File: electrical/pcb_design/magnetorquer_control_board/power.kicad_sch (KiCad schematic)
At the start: 10 parts, among them J4 External Power, U5 INA260, U6 TLV76733DRVx

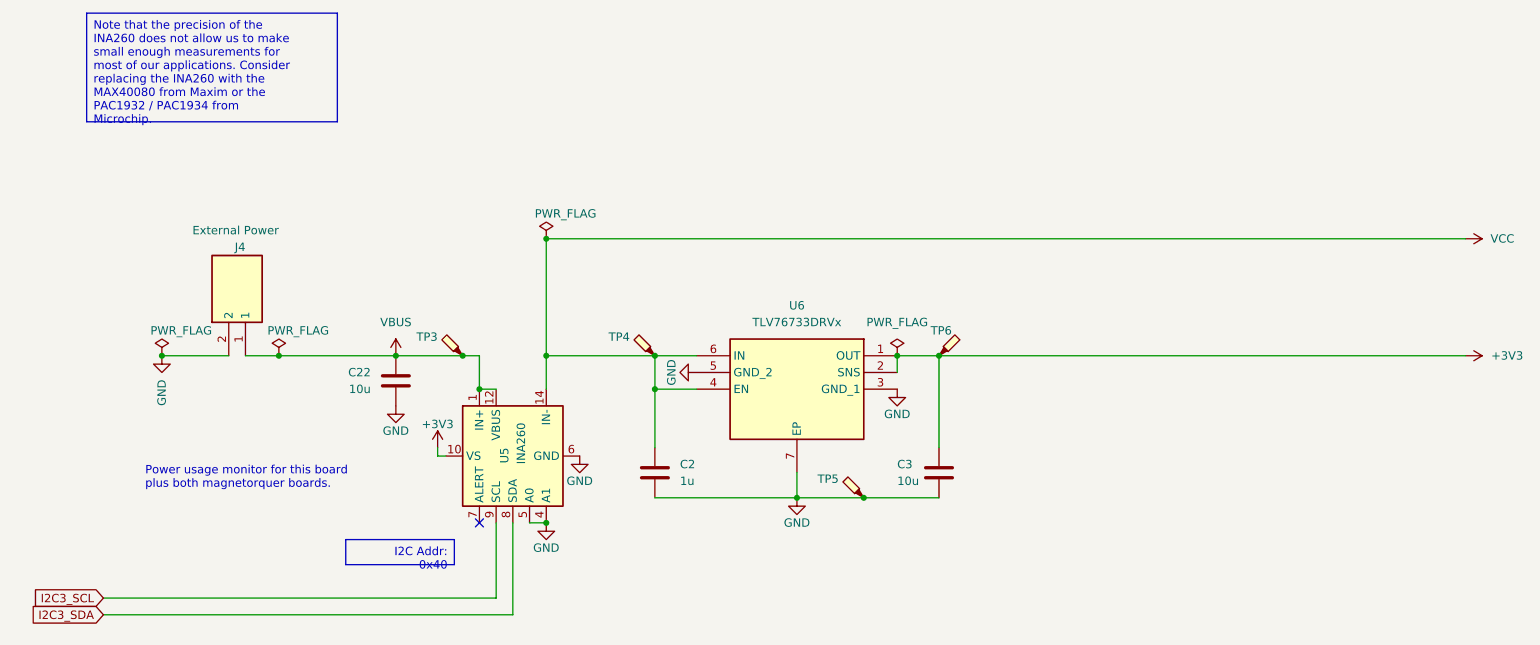
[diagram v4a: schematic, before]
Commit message: Restructure schematic pages. Update designs based on discussions with team.
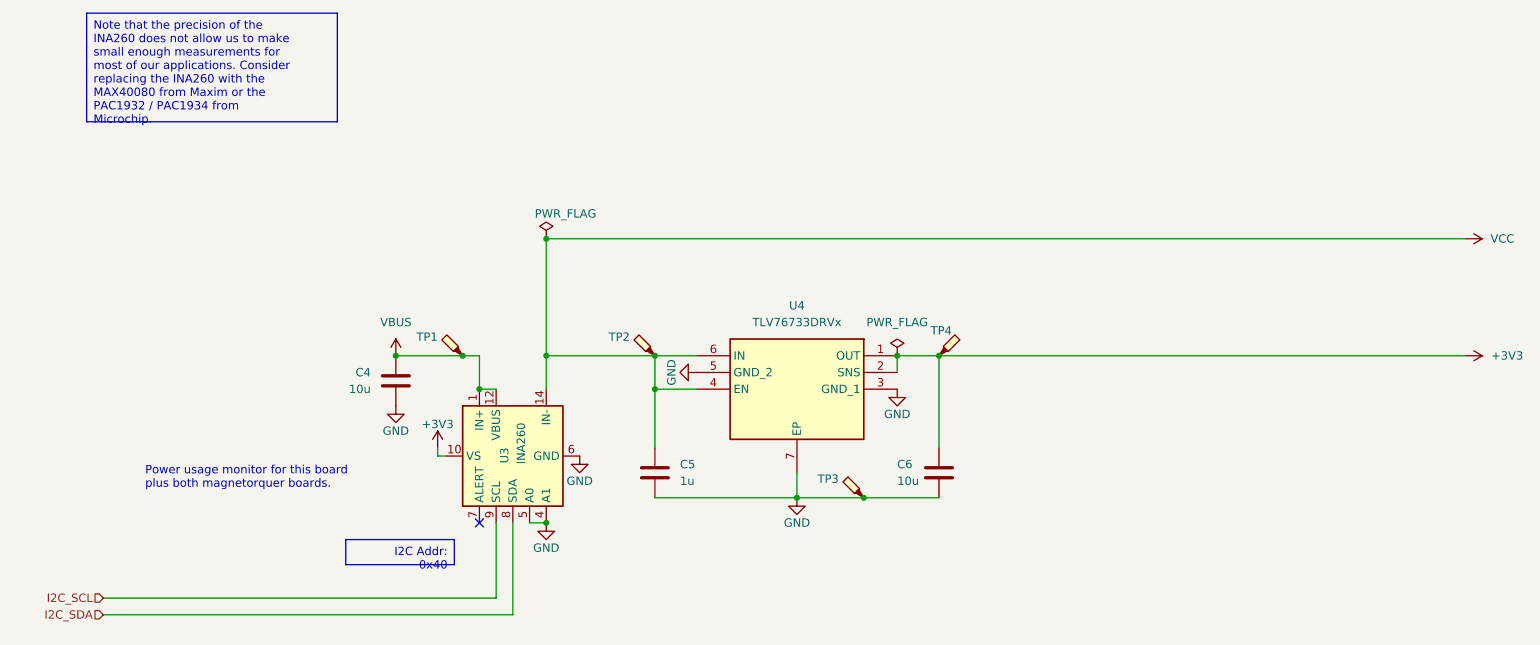
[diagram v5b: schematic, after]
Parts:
- removed J4: External Power, footprints:B2BPHKSLFSN, symbol TVSC:B2B-PH-K-S__LF__SN_
- TP1: renamed from TP3; footprint footprints:TestPoint_Pad_D2.5mm -> footprints:TestPoint_Pad_D1.5mm; now left out of the parts list
- TP2: renamed from TP4; footprint footprints:TestPoint_Pad_D2.5mm -> footprints:TestPoint_Pad_D1.5mm; now left out of the parts list
- TP3: renamed from TP5; footprint footprints:TestPoint_Pad_D2.5mm -> footprints:TestPoint_Pad_D1.5mm; now left out of the parts list
- TP4: renamed from TP6; footprint footprints:TestPoint_Pad_D2.5mm -> footprints:TestPoint_Pad_D1.5mm; now left out of the parts list
- renumbered C22 to C4, C2 to C5, C3 to C6, U5 to U3, U6 to U4
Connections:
- net I2C3_SCL renamed I2C_SCL
- net I2C3_SDA renamed I2C_SDA

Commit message: Update schematic values and add silkscreen text to document solder jumpers, headers, and select ICs. Tweak zones and traces.
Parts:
- TP1: value TestPoint_Probe -> VBUS
- TP2: value TestPoint_Probe -> VCC
- TP3: value TestPoint_Probe -> GND
- TP4: value TestPoint_Probe -> +3V3
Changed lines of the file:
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@@
 			)
 		)
-		(property "Value" "TestPoint_Probe"
+		(property "Value" "VBUS"
 			(at 95.25 70.8025 0)
 			(effects
@@
 			)
 		)
-		(property "Value" "TestPoint_Probe"
+		(property "Value" "VCC"
 			(at 124.46 70.8025 0)
 			(effects
@@
 			)
 		)
-		(property "Value" "TestPoint_Probe"
+		(property "Value" "+3V3"
 			(at 175.26 70.8025 0)
 			(effects
@@
 			)
 		)
-		(property "Value" "TestPoint_Probe"
+		(property "Value" "GND"
 			(at 156.21 92.3925 0)
 			(effects

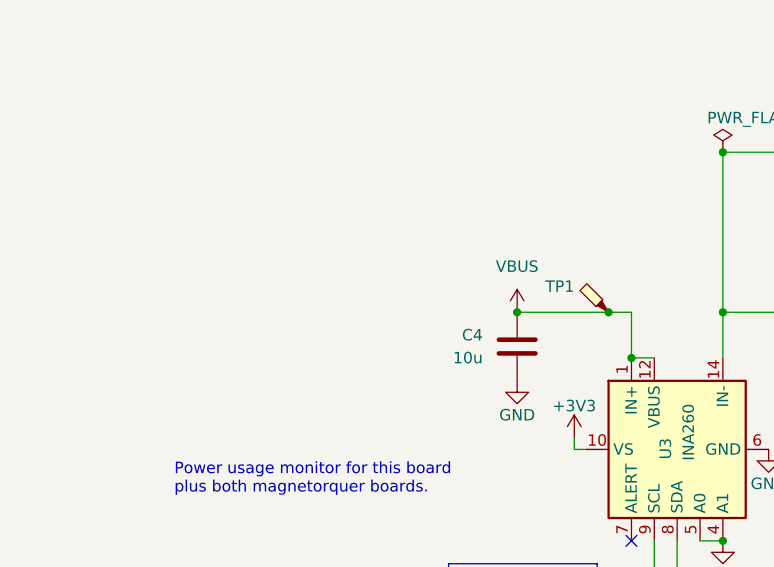
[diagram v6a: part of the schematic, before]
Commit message: Add thank you text and update 3D model.
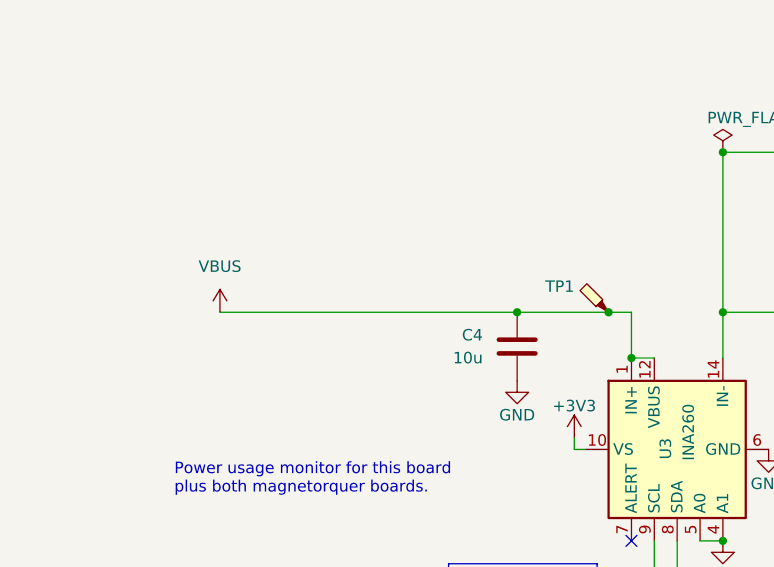
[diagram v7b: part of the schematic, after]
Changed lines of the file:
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@@
+	(wire
+		(pts
+			(xy 55.88 71.12) (xy 88.9 71.12)
+		)
+		(stroke
+			(width 0)
+			(type default)
+		)
+	)
 	(wire
 		(pts
@@
 	(symbol
 		(lib_id "power:VBUS")
-		(at 88.9 71.12 0)
+		(at 55.88 71.12 0)
 		(unit 1)
 		(exclude_from_sim no)
@@
 		(fields_autoplaced yes)
 		(property "Reference" "#PWR14"
-			(at 88.9 74.93 0)
+			(at 55.88 74.93 0)
 			(effects
 				(font
@@
 		)
 		(property "Value" "VBUS"
-			(at 88.9 66.04 0)
+			(at 55.88 66.04 0)
 			(effects
 				(font
@@
 		)
 		(property "Footprint" ""
-			(at 88.9 71.12 0)
+			(at 55.88 71.12 0)
 			(effects
 				(font
@@
 		)
 		(property "Datasheet" ""
-			(at 88.9 71.12 0)
+			(at 55.88 71.12 0)
 			(effects
 				(font
@@
 		)
 		(property "Description" ""
-			(at 88.9 71.12 0)
-			(effects
-				(font
+			(at 55.88 71.12 0)
+			(effects
+				(font

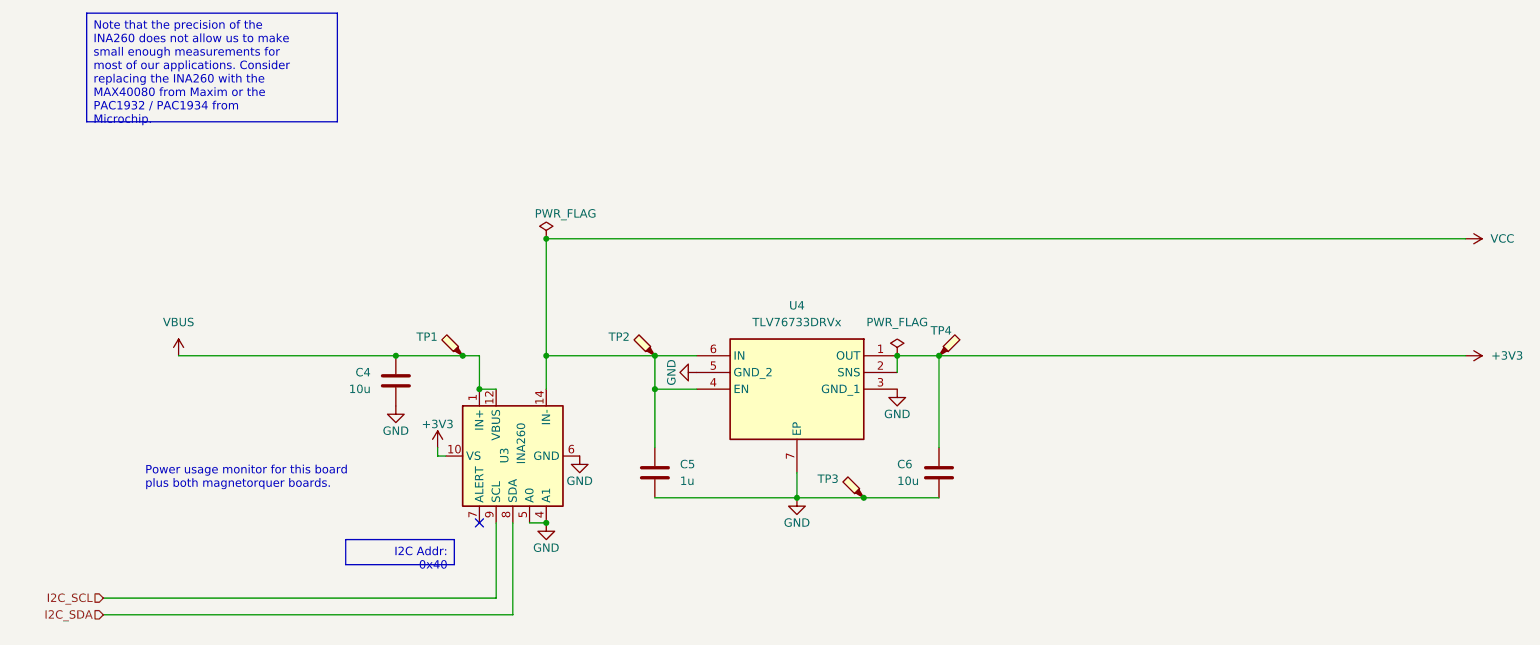
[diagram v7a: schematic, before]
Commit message: Switch from TLV73733DVRT to TPS63900 for voltage regulation. The new part is a buck-boost regulator and will boost the voltage if it is lower than the target.
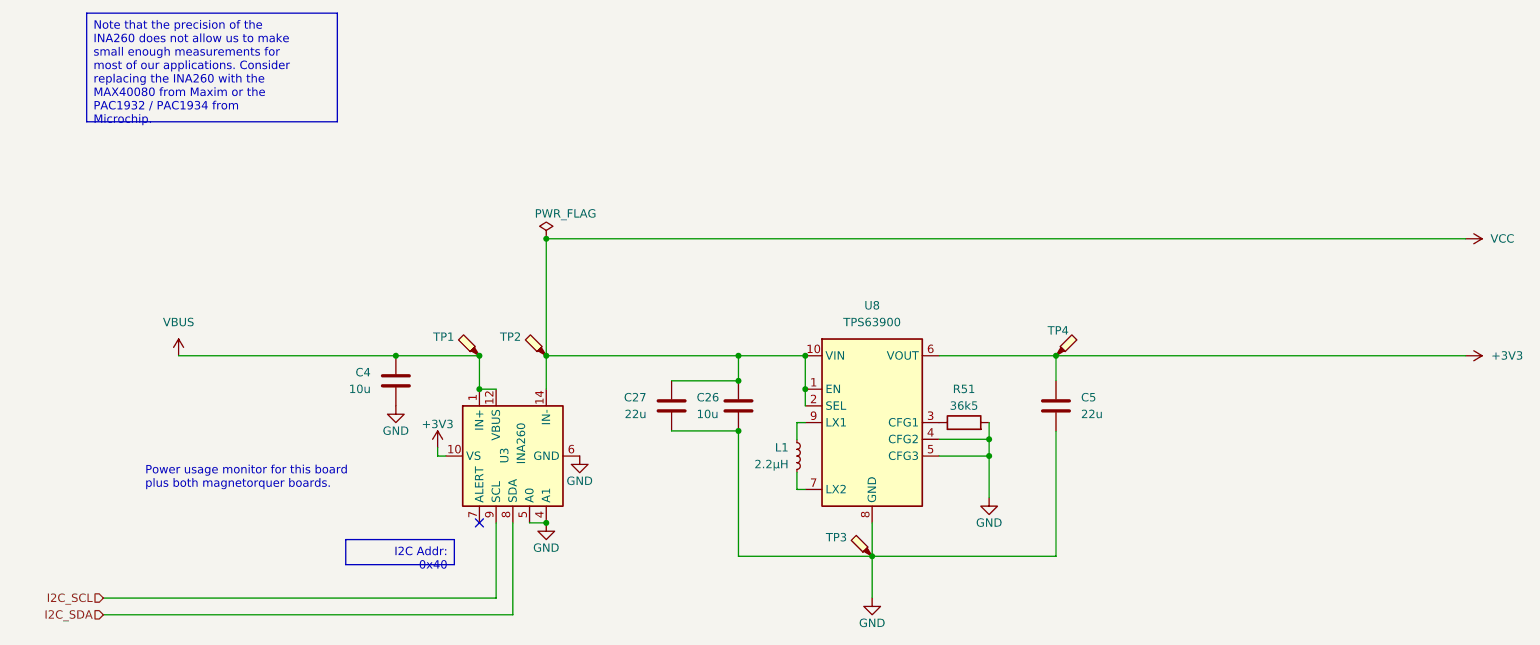
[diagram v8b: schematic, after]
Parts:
- removed C6: 10u, footprints:Nondescript_C_0402_1005Metric, symbol Device:C
- removed U4: TLV76733DRVx, footprints:SON65P200X200X80-7N, symbol TVSC:TLV76733DRVT
- added C26: 10u, footprints:Nondescript_C_0603_1608Metric, symbol Device:C
- added C27: 22u, footprints:Nondescript_C_0603_1608Metric, symbol Device:C
- added L1: 2.2µH, Inductor_SMD:L_1008_2520Metric, symbol Device:L_Small
- added R51: 36k5, footprints:Nondescript_R_0603_1608Metric, symbol Device:R
- added U8: TPS63900, Package_SON:WSON-10-1EP_2.5x2.5mm_P0.5mm_EP1.2x2mm, symbol Regulator_Switching:TPS63900
- C4: footprint footprints:Nondescript_C_0402_1005Metric -> footprints:Nondescript_C_0603_1608Metric; Basic or Extended Component Basic -> Extended; MPN C15525 -> C77041; Manufacturer Samsung Electro-Mechanics -> Murata; Manufacturer Part Number CL05A106MQ5NUNC -> GRM188R60J106ME47D
- C5: value 1u -> 22u; footprint footprints:Nondescript_C_0402_1005Metric -> footprints:Nondescript_C_0603_1608Metric; Basic or Extended Component Basic -> Extended; MPN C52923 -> C710887; Manufacturer Samsung Electro-Mechanics -> Murata; Manufacturer Part Number CL05A105KA5NQNC -> GRM187R60J226ME15D
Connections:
- net +3V3: now also C5.1, U8.6 (VOUT)
- net GND: now also C26.2, C27.2, R51.2, U8.11 (GND), U8.4 (CFG2), U8.5 (CFG3), U8.8 (GND)
- net VCC: now also C26.1, C27.1, U8.1 (EN), U8.10 (VIN), U8.2 (SEL); no longer C5.1
- new net: L1.1, U8.7 (LX2)
- new net: L1.2, U8.9 (LX1)
- new net: R51.1, U8.3 (CFG1)
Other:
- moved on the sheet: TP1
